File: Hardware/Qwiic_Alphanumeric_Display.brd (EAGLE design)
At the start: 160 x 100 mm, 16 parts, among them J1 PTH, J2 Qwiic Right Angle, U2 HT16K33

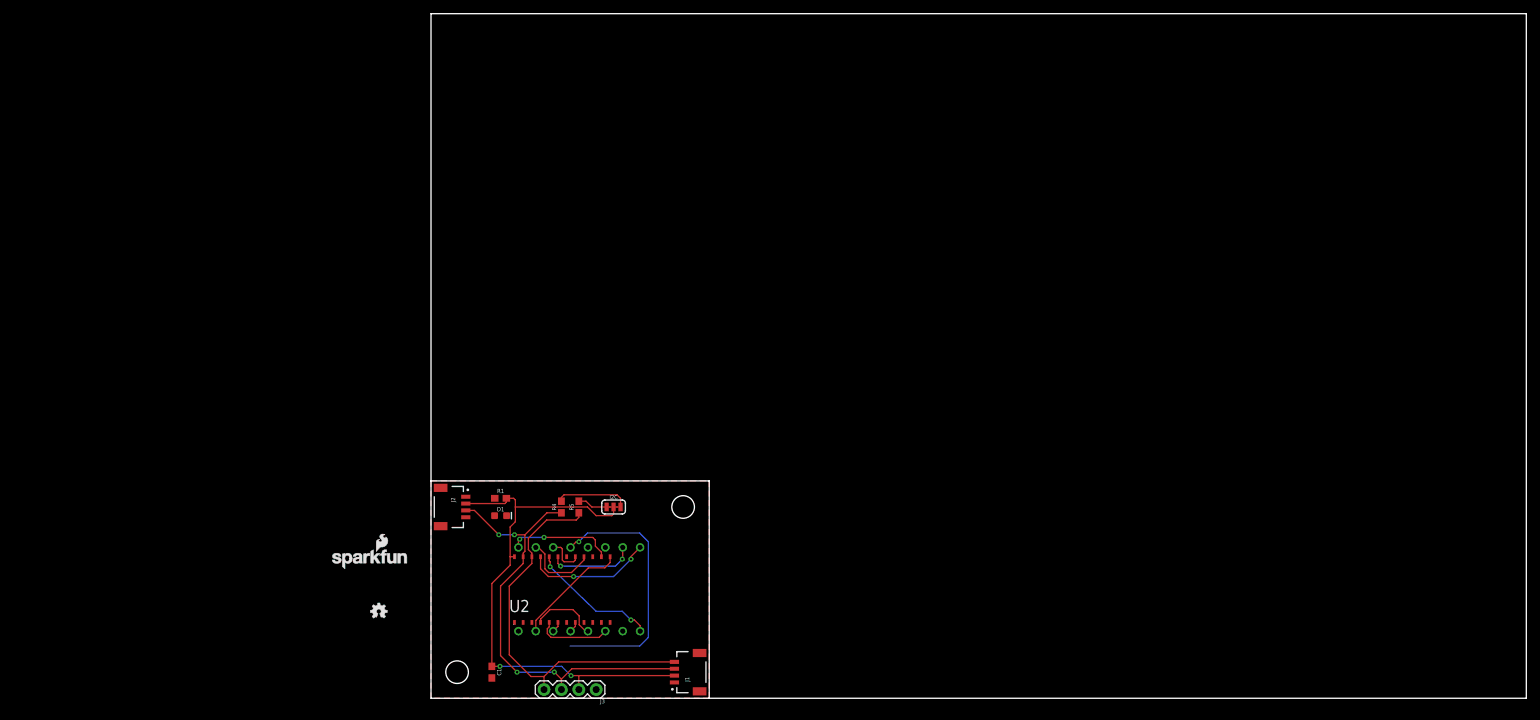
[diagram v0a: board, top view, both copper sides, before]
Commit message: New Board Layout
The pins were remapped with the LED Driver and the Display to create a better board layout.
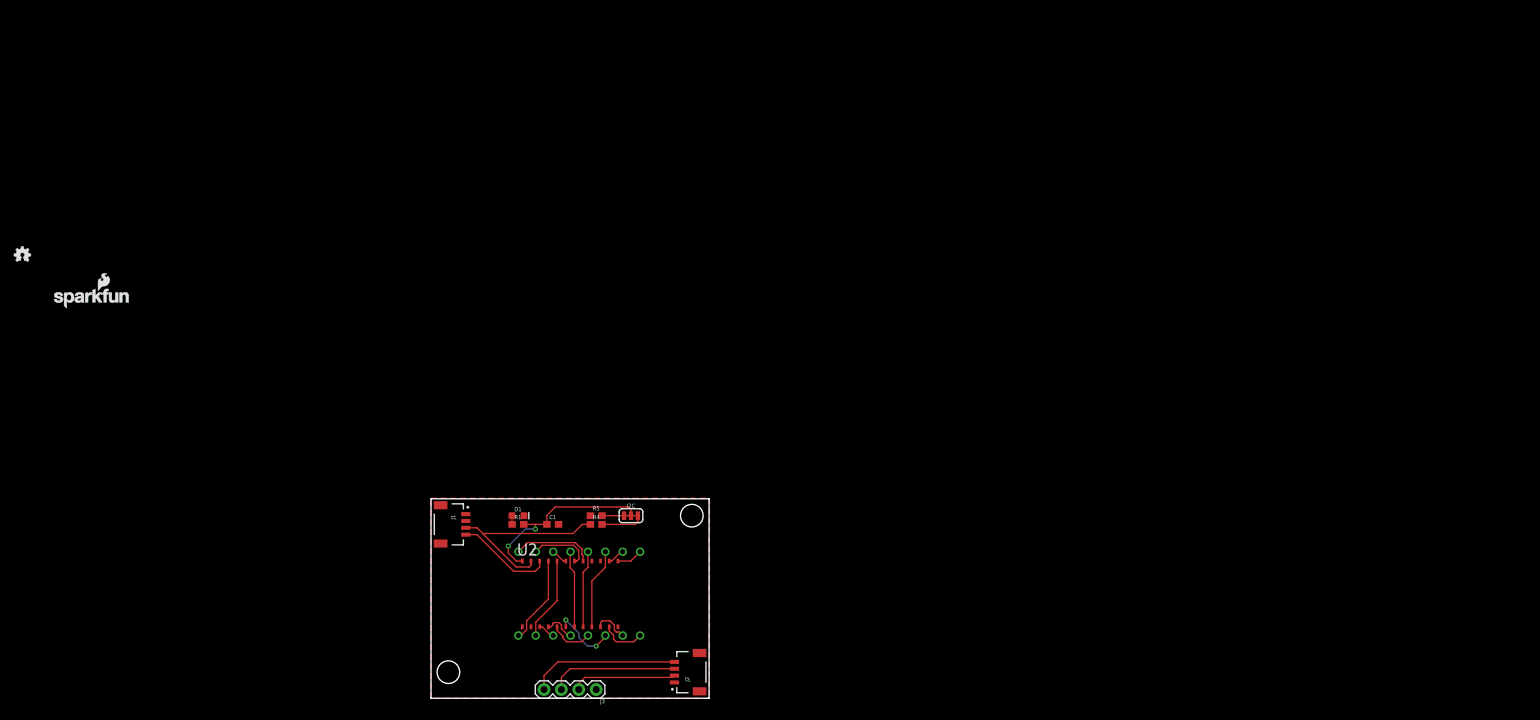
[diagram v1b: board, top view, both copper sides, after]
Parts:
- moved FRAME1 95.2 mm to (-80.0, 48.3)
- moved LOGO1 73.6 mm to (-59.7, 64.8)
- moved LOGO2 55.7 mm to (-49.5, 58.4)
- moved JP1 41.9 mm to (2.54, 3.81), flipped to the bottom
- moved JP8 41.2 mm to (38.1, 26.7)
- moved J2 38.9 mm to (35.6, 3.81), turned to 90 degrees
- moved J1 37.4 mm to (5.08, 25.4), turned to 270 degrees
- moved C1 23.3 mm to (17.8, 25.4), turned to 0 degrees
- moved R4 5.68 mm to (24.1, 25.4), turned to 0 degrees
- moved R1 4.58 mm to (12.7, 25.4)
- moved I2C 2.84 mm to (29.2, 26.7)
- moved R5 2.84 mm to (24.1, 26.7), turned to 0 degrees
- moved D1 2.54 mm to (12.7, 26.7)
- moved U2 1.31 mm to (20.3, 15.2)
- moved U1 0.63 mm to (21.3, 14.9)
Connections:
- net COM_A: now also U2.9; no longer U2.2
- net COM_B: now also U2.8; no longer U2.3
- net COM_C: now also U2.5; no longer U2.4
- net COM_D: now also U2.6; no longer U2.5
- net COM_E: now also U2.3; no longer U2.6
- net COM_G1: now also U2.4; no longer U2.8
- net DIG_1A: now also U2.13; no longer U2.21
- net DIG_1B: now also U2.11; no longer U2.20
- net DIG_2A: now also U2.14; no longer U2.19
- net DIG_2B: now also U2.10; no longer U2.18
- net DIG_3A: now also U2.19; no longer U2.17
- net DIG_3B: now also U2.18; no longer U2.16
- net DIG_4A: now also U2.21; no longer U2.15
- net DIG_4B: now also U2.17; no longer U2.14
- net DIG_DP: now also U2.20; no longer U2.13
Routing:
- net 3.3V: track 79.6 -> 43.0 mm
- net COM_F: track 38.7 -> 11.3 mm, vias 1 -> 0
- net SCL: track 56.1 -> 36.1 mm
- net SDA: track 64.9 -> 47.7 mm, vias 4 -> 0
- net DIG_1A: track 18.8 -> 3.81 mm, vias 2 -> 0
- net DIG_4A: track 0.00 -> 12.9 mm
- net DIG_1B: track 19.0 -> 6.48 mm, vias 2 -> 0
- net COM_A: track 0.00 -> 11.8 mm
- net COM_B: track 0.00 -> 11.3 mm
- net DIG_2A: track 12.7 -> 2.54 mm, vias 2 -> 0
- net DIG_2B: track 0.00 -> 5.29 mm
- net DIG_DP: track 16.8 -> 12.2 mm
- net N$5: track 10.8 -> 6.29 mm
- net COM_C: track 10.0 -> 6.25 mm
- net DIG_4B: track 15.4 -> 12.0 mm, vias 2 -> 0
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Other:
- board size 160 x 100 mm -> 40.6 x 29.1 mm

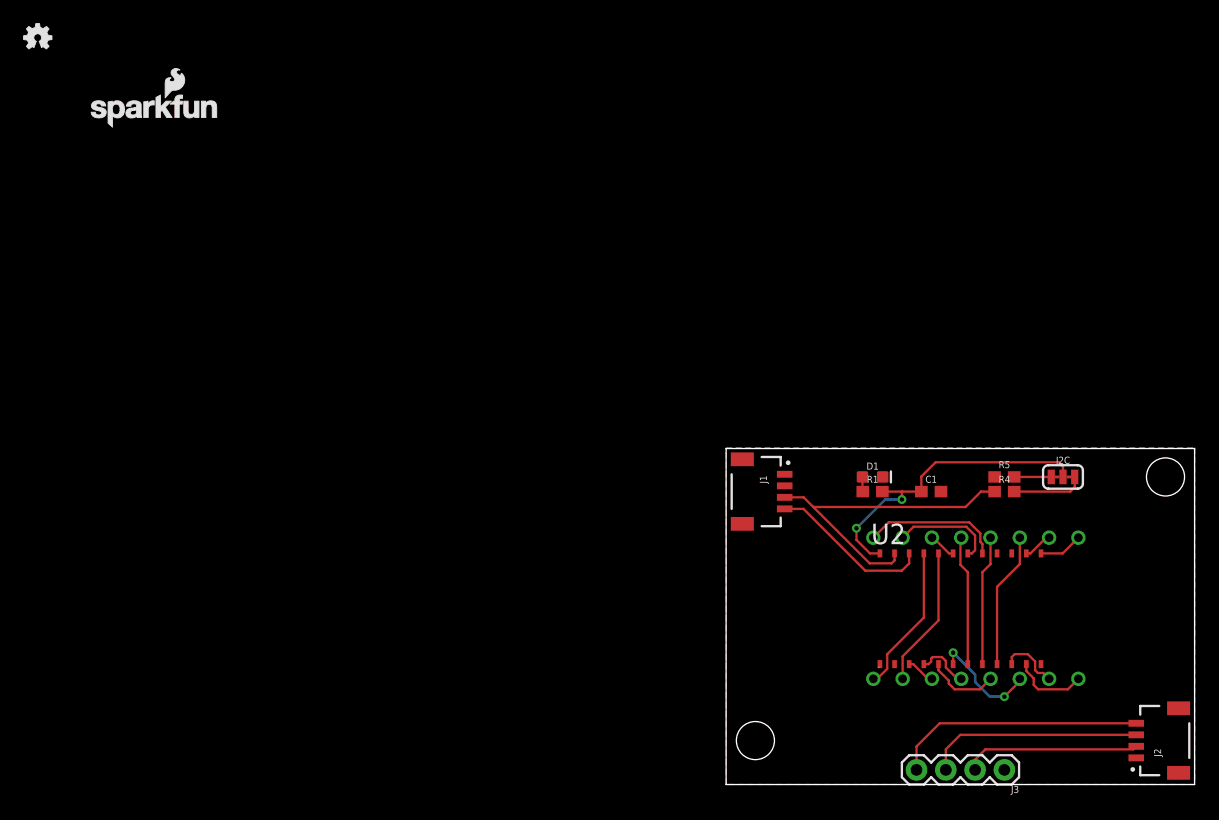
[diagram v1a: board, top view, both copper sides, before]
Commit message: Created new Board
Recreated the board in the new Branch with different pin mappings between the HT16K33 and the LED Display for easier routing
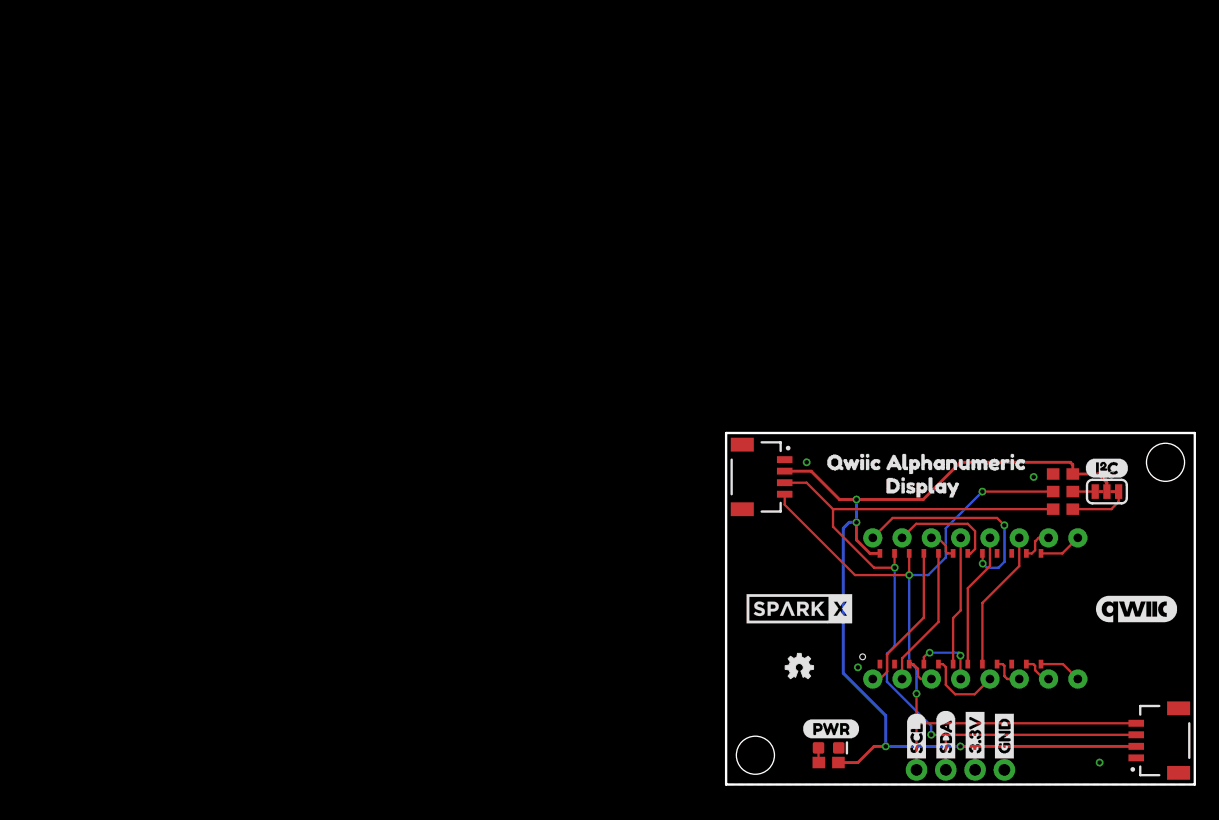
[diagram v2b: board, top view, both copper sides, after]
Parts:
- removed LOGO2: SFE_LOGO_NAME_FLAME.1_INCH, SparkFun-Aesthetics:SFE_LOGO_NAME_FLAME_.1
- added U$1, U$6: (no value), buzzard_labels:3#3V1
- added U$10: (no value), Labels:I_SUPER2_C-()-04
- added U$11: (no value), Labels:QWIIC_COPYRIGHT_MEDIUM
- added U$12, U$14: (no value), SparkX:SPARKX-MEDIUM
- added U$15: (no value), buzzard_labels (4):QWIIC_ALPHANUMERIC0
- added U$16: (no value), buzzard_labels (4):DISPLAY1
- added U$2, U$7: (no value), buzzard_labels:GND0
- added U$3: (no value), buzzard_labels:PWR5
- added U$4, U$8: (no value), buzzard_labels:SCL3
- added U$5, U$9: (no value), buzzard_labels:SDA2
- J3: device SparkFun-Connectors:1X04 -> SparkFun-Connectors:1X04_NO_SILK
- moved FRAME1 97.3 mm to (-1.27, -8.89)
- moved LOGO1 85.7 mm to (6.35, 10.2)
- moved D1 23.8 mm to (8.89, 3.17)
- moved R1 23.8 mm to (8.89, 1.91)
- moved C1 11.5 mm to (29.2, 26.9), turned to 180 degrees
- moved R4 5.30 mm to (29.2, 23.9)
- moved R5 5.24 mm to (29.2, 25.4)
- moved I2C 4.02 mm to (33.0, 25.4)
- moved J1 1.27 mm to (5.08, 26.7)
- moved JP1 1.27 mm to (2.54, 2.54)
- moved JP8 1.27 mm to (38.1, 27.9)
- moved U1 1.09 mm to (20.3, 15.2)
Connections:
- net COM_A: now also U2.8; no longer U2.9
- net COM_B: now also U2.7; no longer U2.8
- net COM_D: now also U2.9; no longer U2.6
- net COM_F: now also U2.6; no longer U2.7
- net DIG_1B: now also U2.12; no longer U2.11
- net DIG_2B: now also U2.11; no longer U2.10
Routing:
- net 3.3V: track 43.0 -> 88.5 mm, vias 2 -> 4
- net SCL: track 36.1 -> 69.3 mm, vias 0 -> 3
- net SDA: track 47.7 -> 71.0 mm, vias 0 -> 2
- net DIG_4B: track 12.0 -> 18.7 mm, vias 0 -> 2
- net COM_D: track 9.48 -> 2.98 mm, vias 2 -> 0
- net DIG_1B: track 6.48 -> 3.73 mm
- net DIG_2B: track 5.29 -> 2.68 mm
- net COM_G1: track 4.75 -> 6.16 mm, vias 0 -> 2
- net N$4: track 3.21 -> 1.94 mm
- net N$5: track 6.29 -> 5.13 mm
- net COM_C: track 6.25 -> 7.00 mm
- added copper zone on layer 16, net GND
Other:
- board size 40.6 x 29.1 mm -> 40.6 x 30.5 mm
- board text added: "Madison Chodikov"

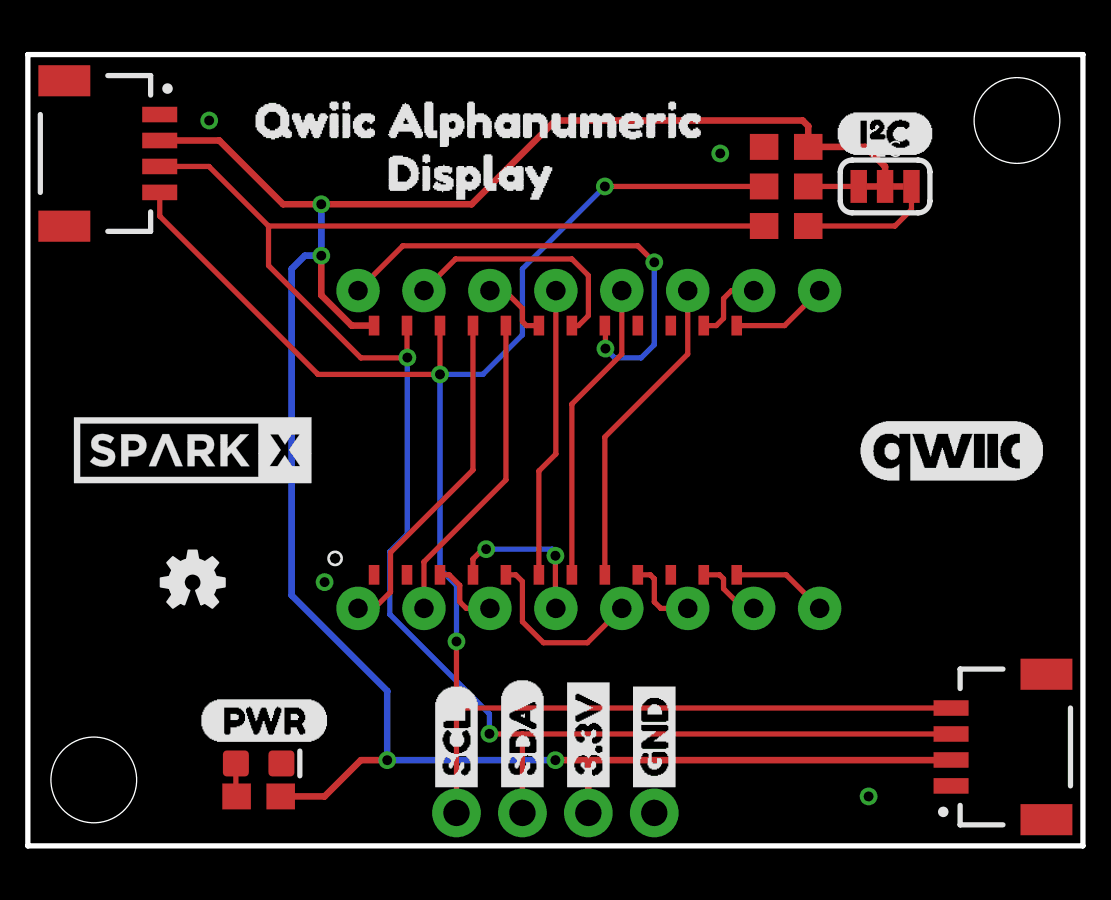
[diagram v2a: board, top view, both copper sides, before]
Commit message: Added Panelized Board and Gerber Files
Updated the HT16K33 Footprint, fixed the board files to match the footprint, added the panelized production board and gerber files for ordering the board
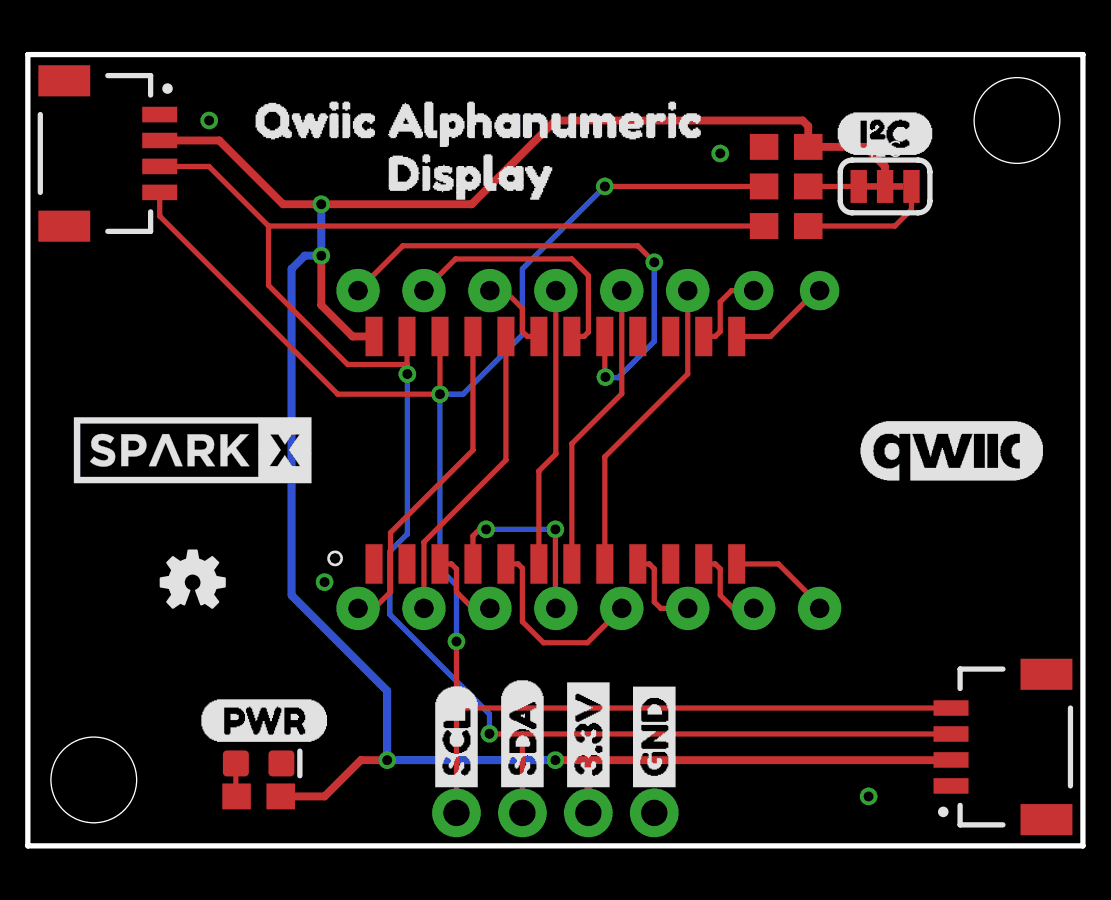
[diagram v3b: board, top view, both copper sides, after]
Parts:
- added U$13: (no value), buzzard_labels (4):QWIIC_ALPHANUMERIC0
- added U$17: (no value), buzzard_labels (4):DISPLAY1
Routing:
- net COM_G1: track 6.16 -> 7.41 mm
- net DIG_4B: track 18.7 -> 19.5 mm
- net DIG_2B: track 2.68 -> 3.23 mm
- net DIG_3B: track 9.44 -> 9.99 mm
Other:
- board text added: "I2C"
- board text added: "U1"

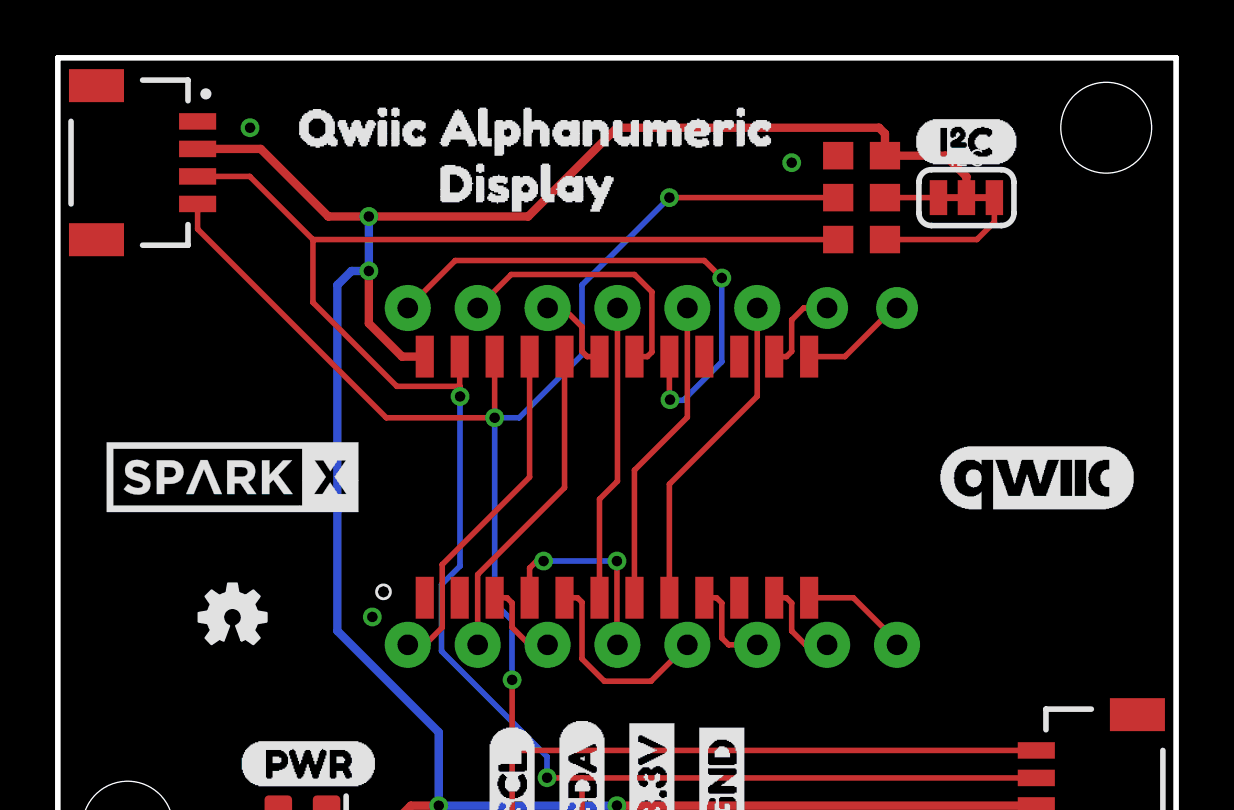
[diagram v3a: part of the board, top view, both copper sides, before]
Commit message: Moved Decoupling Cap
Moved the decoupling capacitor next to the LED driver to resolve the GitHub issue
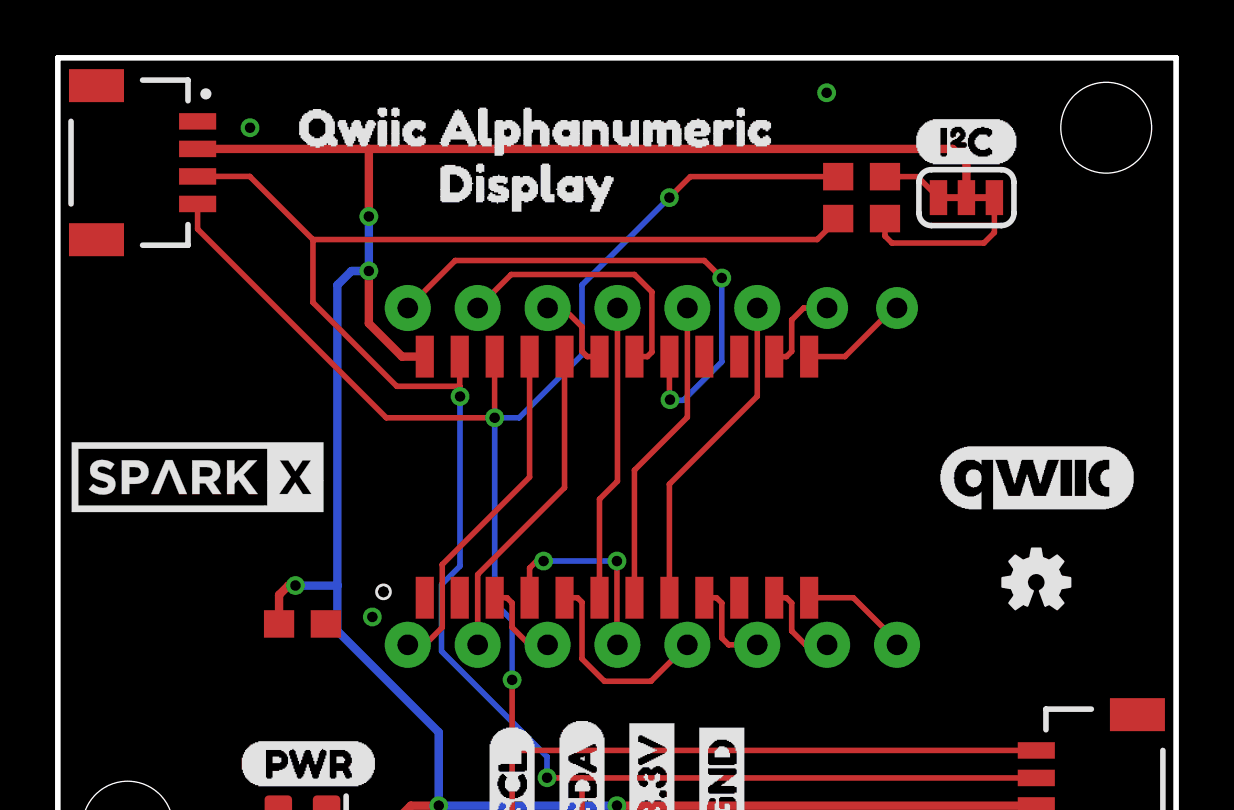
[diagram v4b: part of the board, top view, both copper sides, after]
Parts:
- moved LOGO1 29.2 mm to (35.6, 11.4)
- moved C1 26.5 mm to (8.89, 9.91), turned to 0 degrees
- moved U$12 1.27 mm to (5.08, 15.2)
- moved R4 0.76 mm to (29.2, 24.6)
- moved R5 0.76 mm to (29.2, 26.2)
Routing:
- net 3.3V: track 88.9 -> 91.8 mm, vias 4 -> 5
- net N$5: track 5.13 -> 6.14 mm
